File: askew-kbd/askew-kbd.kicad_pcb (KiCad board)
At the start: 2 copper layers, 155.6 x 108.4 mm, 68 parts, among them J1 OLED, J2 MJ-4PP-9, SW1 SW_PUSH, SW10 SW_PUSH, SW11 SW_PUSH, SW12 SW_PUSH, SW13 SW_PUSH, SW14 SW_PUSH, SW15 SW_PUSH, SW16 SW_PUSH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

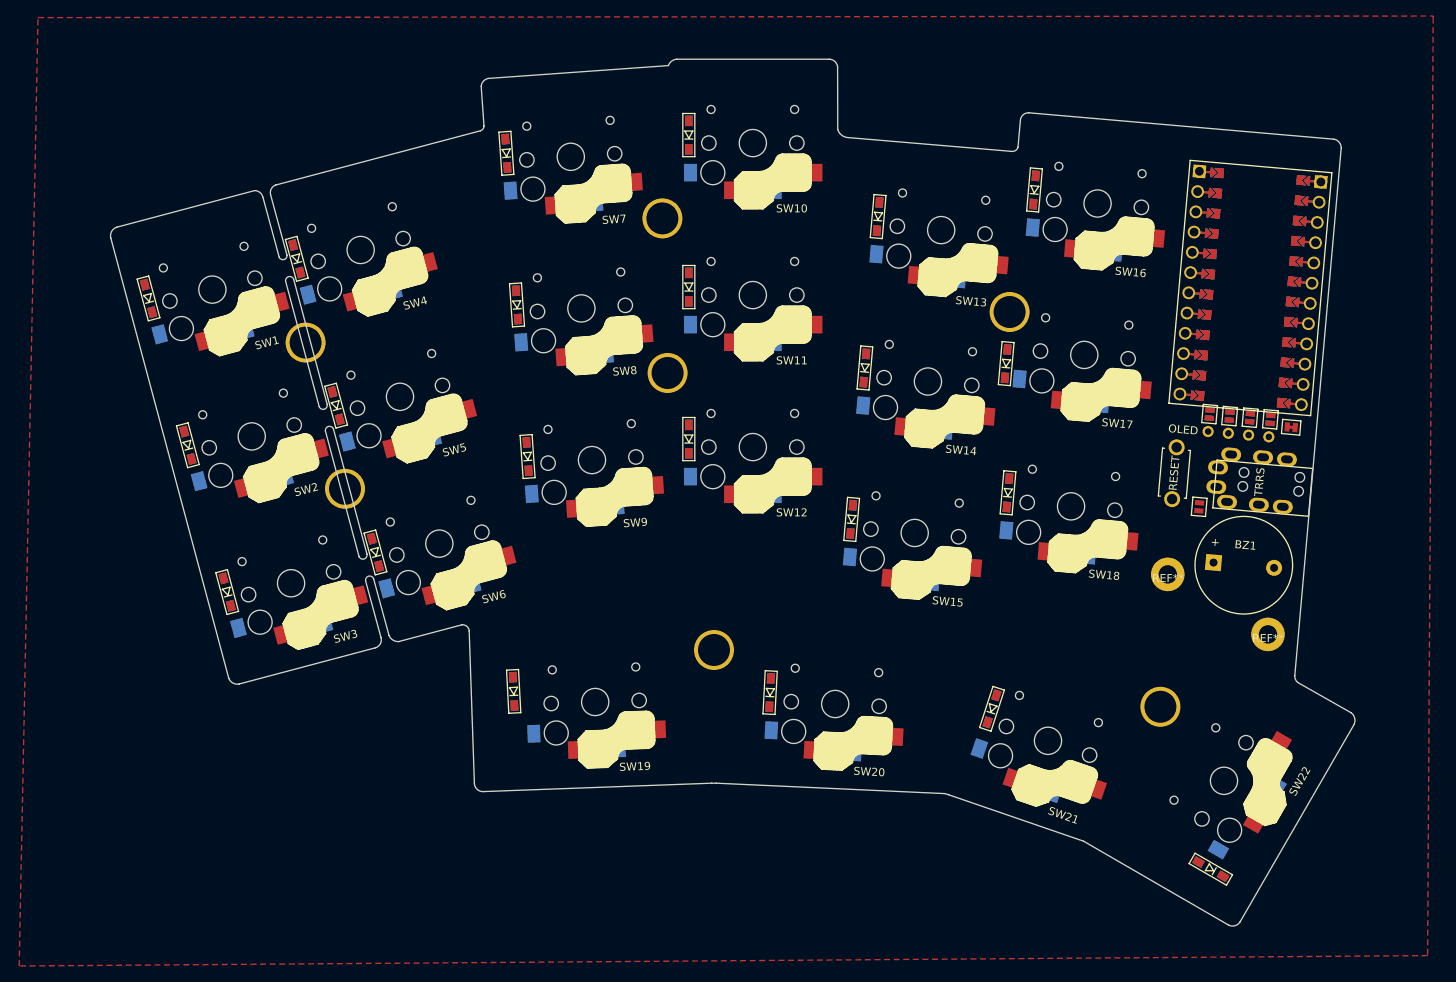
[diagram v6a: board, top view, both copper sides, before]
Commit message: remove buzzer and add diodes silk
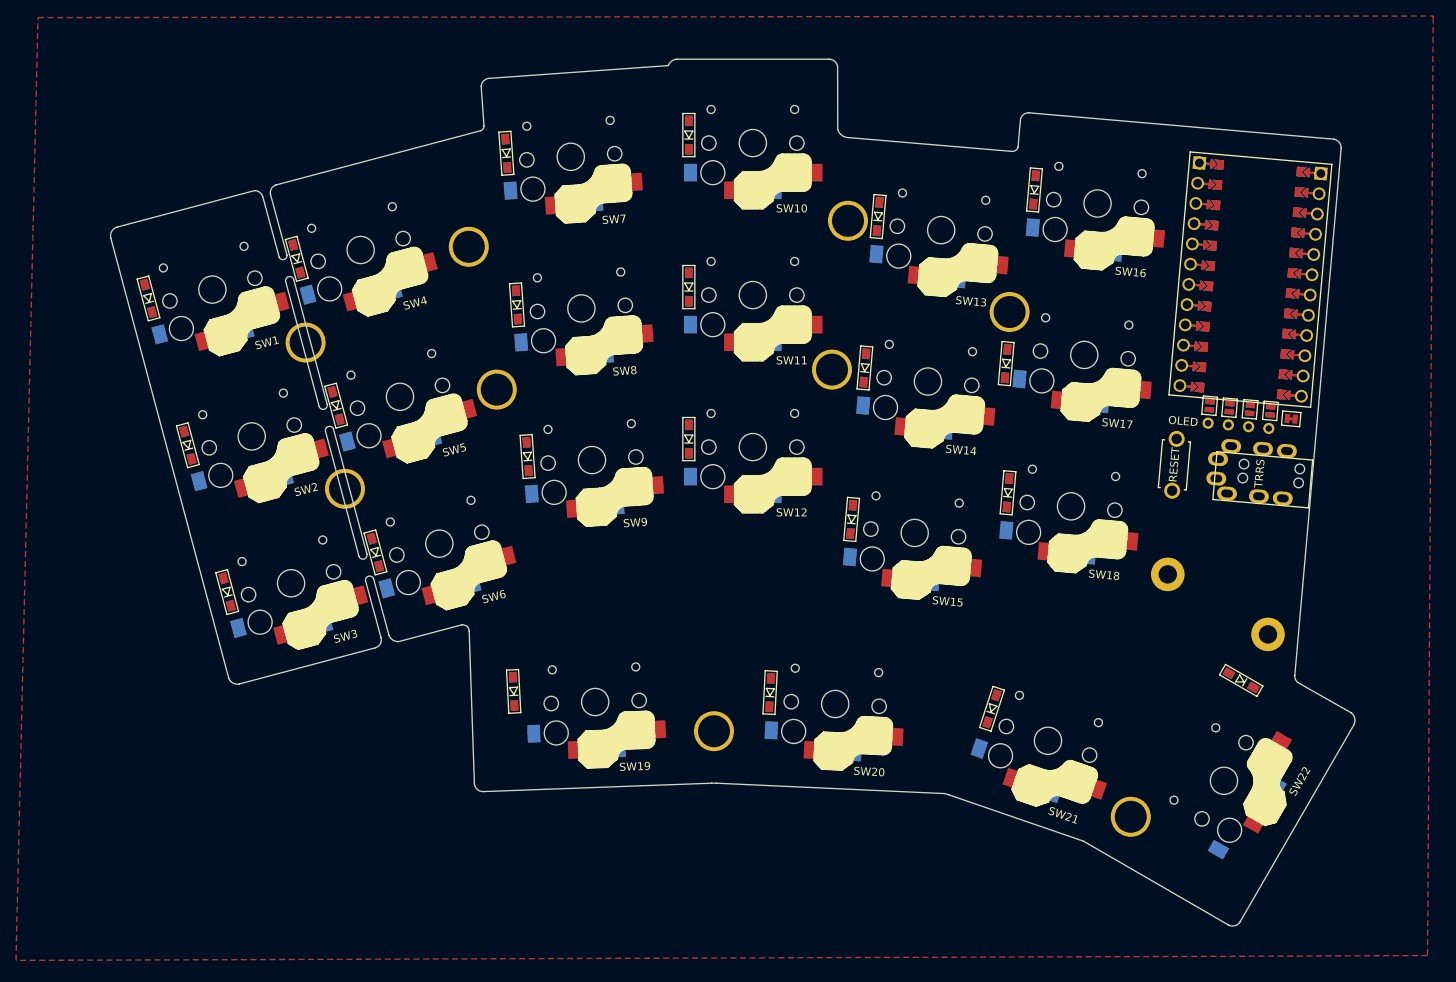
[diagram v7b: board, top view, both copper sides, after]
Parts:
- removed BZ1: Buzzer, Buzzer_Beeper:Buzzer_12x9.5RM7.6
- removed JP10: , kbd:Jumper
- added REF**: M2_Hole_TH_Outside, kbd:M2_Hole_TH_Outside, F.Cu at (109.1, 92.1)
- added REF**: M2_Hole_TH_Outside, kbd:M2_Hole_TH_Outside, F.Cu at (105.6, 74.2)
- D1, D10, D11, D12, D13, D14, D15, D16, D17, D18, D19, D2, D20, D21, D22, D3, D4, D5, D6, D7, D8, D9: footprint kbd:D3_SMD -> fp:D3_SMD
- moved D22 23.9 mm to (202.2, 128.4)
- moved REF** 23.2 mm to (153.0, 71.0)
- moved REF** 20.6 mm to (151.0, 89.6)
- moved REF** 14.2 mm to (188.3, 145.5)
- moved REF** 10.2 mm to (136.2, 134.8)
- moved JP1 1.05 mm to (205.8, 94.8)
- moved JP5 1.05 mm to (205.8, 94.8)
- moved U1 1.05 mm to (203.3, 78.3)
- moved J1 1.05 mm to (201.8, 96.6)
- moved J2 1.05 mm to (210.8, 103.9)
- moved JP2 1.05 mm to (203.3, 94.6)
- moved JP3 1.05 mm to (200.7, 94.4)
- moved JP4 1.05 mm to (198.2, 94.1)
- moved JP6 1.05 mm to (203.3, 94.6)
- moved JP7 1.05 mm to (200.7, 94.4)
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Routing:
- net GND: track 0.00 -> 0.52 mm
- net (no net): track 0.52 -> 0.00 mm

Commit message: add rotary
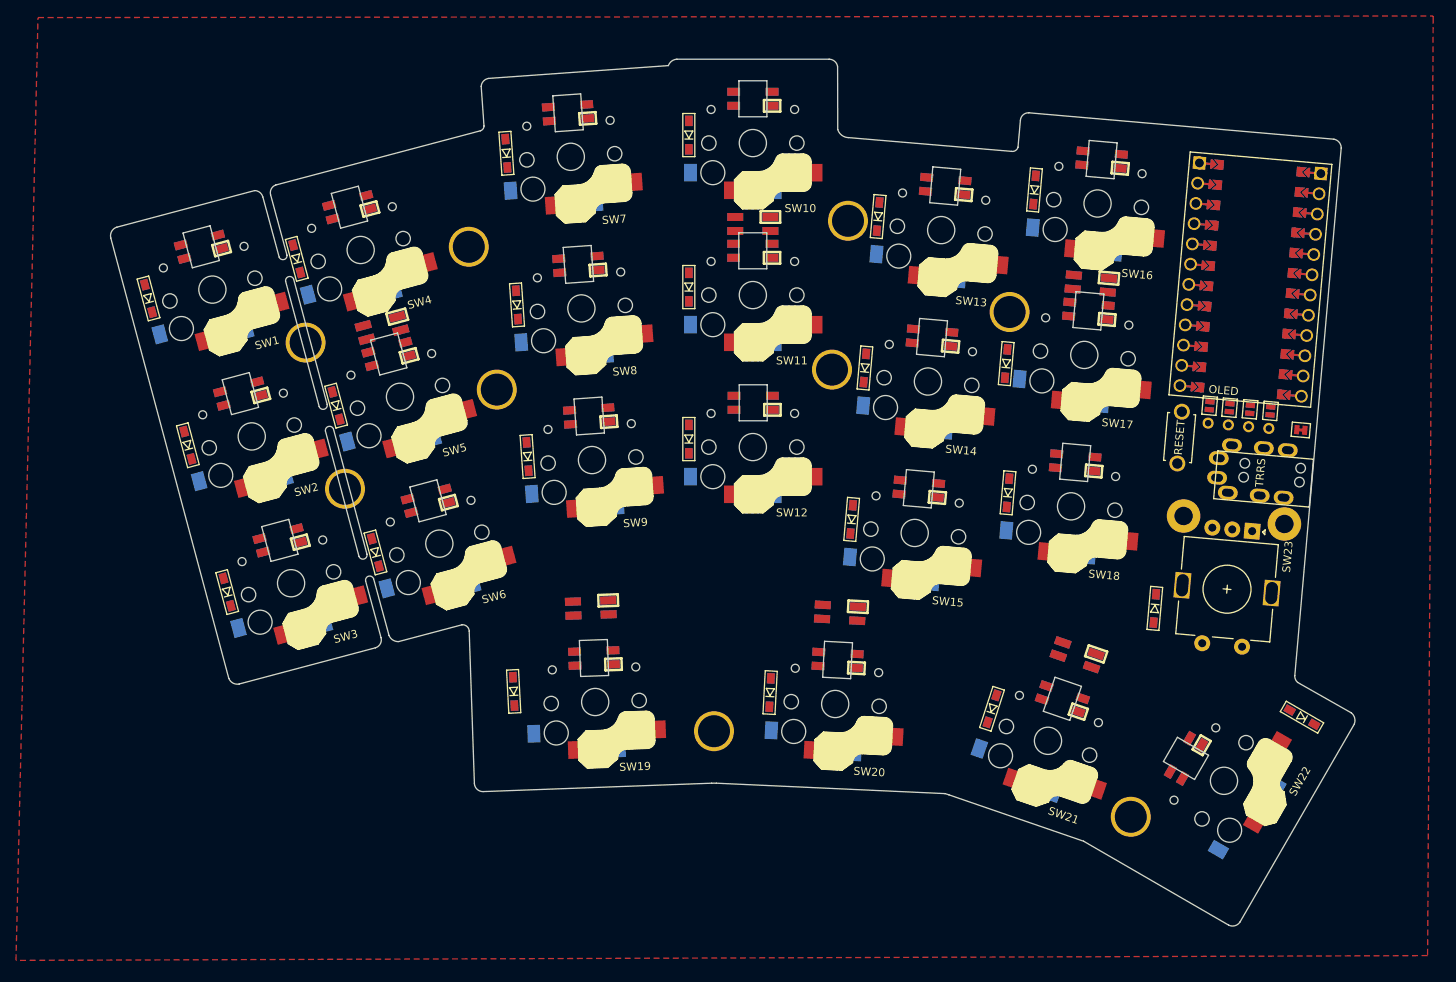
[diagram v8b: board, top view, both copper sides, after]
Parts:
- added D23: DIODE, fp:D3_SMD, F.Cu at (191.3, 119.5)
- added L1: SK6812MINI, fp:SK6812MINI_rev, F.Cu at (72.2, 74.2)
- added L10: SK6812MINI, fp:SK6812MINI_rev, F.Cu at (141.1, 55.8)
- added L11: SK6812MINI, fp:SK6812MINI_rev, F.Cu at (141.1, 74.8)
- added L12: SK6812MINI, fp:SK6812MINI_rev, F.Cu at (141.2, 93.8)
- added L13: SK6812MINI, fp:SK6812MINI_rev, F.Cu at (165.2, 66.7)
- added L14: SK6812MINI, fp:SK6812MINI_rev, F.Cu at (163.5, 85.6)
- added L15: SK6812MINI, fp:SK6812MINI_rev, F.Cu at (161.8, 104.5)
- added L16: SK6812MINI, fp:SK6812MINI_rev, F.Cu at (184.7, 63.4)
- added L17: SK6812MINI, fp:SK6812MINI_rev, F.Cu at (183.1, 82.2)
- added L18: SK6812MINI, fp:SK6812MINI_rev, F.Cu at (181.4, 101.2)
- added L19: SK6812MINI, fp:SK6812MINI_rev, F.Cu at (121.2, 125.7)
- added L2: SK6812MINI, fp:SK6812MINI_rev, F.Cu at (77.0, 92.6)
- added L20: SK6812MINI, fp:SK6812MINI_rev, F.Cu at (151.7, 125.9)
- added L21: SK6812MINI, fp:SK6812MINI_rev, F.Cu at (179.8, 130.8)
- added L22: SK6812MINI, fp:SK6812MINI_rev, F.Cu at (195.2, 138.2)
- added L23: SK6812MINI, fp:SK6812MINI_underglow_rev, F.Cu at (181.7, 125.2)
- added L24: SK6812MINI, fp:SK6812MINI_underglow_rev, F.Cu at (152.0, 120.0)
- added L25: SK6812MINI, fp:SK6812MINI_underglow_rev, F.Cu at (120.8, 119.4)
- added L26: SK6812MINI, fp:SK6812MINI_underglow_rev, F.Cu at (94.8, 84.4)
- added L27: SK6812MINI, fp:SK6812MINI_underglow_rev, F.Cu at (141.1, 71.4)
- added L28: SK6812MINI, fp:SK6812MINI_underglow_rev, F.Cu at (183.3, 78.8)
- added L3: SK6812MINI, fp:SK6812MINI_rev, F.Cu at (82.0, 111.0)
- added L4: SK6812MINI, fp:SK6812MINI_rev, F.Cu at (90.7, 69.3)
- added L5: SK6812MINI, fp:SK6812MINI_rev, F.Cu at (95.6, 87.7)
- added L6: SK6812MINI, fp:SK6812MINI_rev, F.Cu at (100.5, 106.0)
- added L7: SK6812MINI, fp:SK6812MINI_rev, F.Cu at (118.0, 57.5)
- added L8: SK6812MINI, fp:SK6812MINI_rev, F.Cu at (119.3, 76.5)
- added L9: SK6812MINI, fp:SK6812MINI_rev, F.Cu at (120.7, 95.4)
- added SW23: RotaryEncoder_Switch, Rotary_Encoder:RotaryEncoder_Alps_EC11E-Switch_Vertical_H20mm, F.Cu at (203.5, 109.8)
- moved REF** 14.0 mm to (207.6, 108.9)
- moved D22 8.88 mm to (209.8, 133.1)
- moved REF** 7.56 mm to (194.9, 107.9)
- moved RSW1 3.46 mm to (194.4, 98.1)
- moved JP9 1.84 mm to (209.6, 97.2)
- moved J2 0.14 mm to (210.9, 103.8)
- turned JP4 to -95 degrees
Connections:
- net col1 renamed SW23a
- U1 pad 19: unconnected-(U1-Pad19) -> encoderB
- U1 pad 20: unconnected-(U1-Pad20) -> encoderA
- U1 pad 8: buzzer -> unconnected-(U1-Pad8)
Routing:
- net GND: track 0.52 -> 0.00 mm
